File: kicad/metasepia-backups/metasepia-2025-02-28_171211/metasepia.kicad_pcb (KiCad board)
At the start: 2 copper layers, 227.4 x 131.5 mm, 63 parts

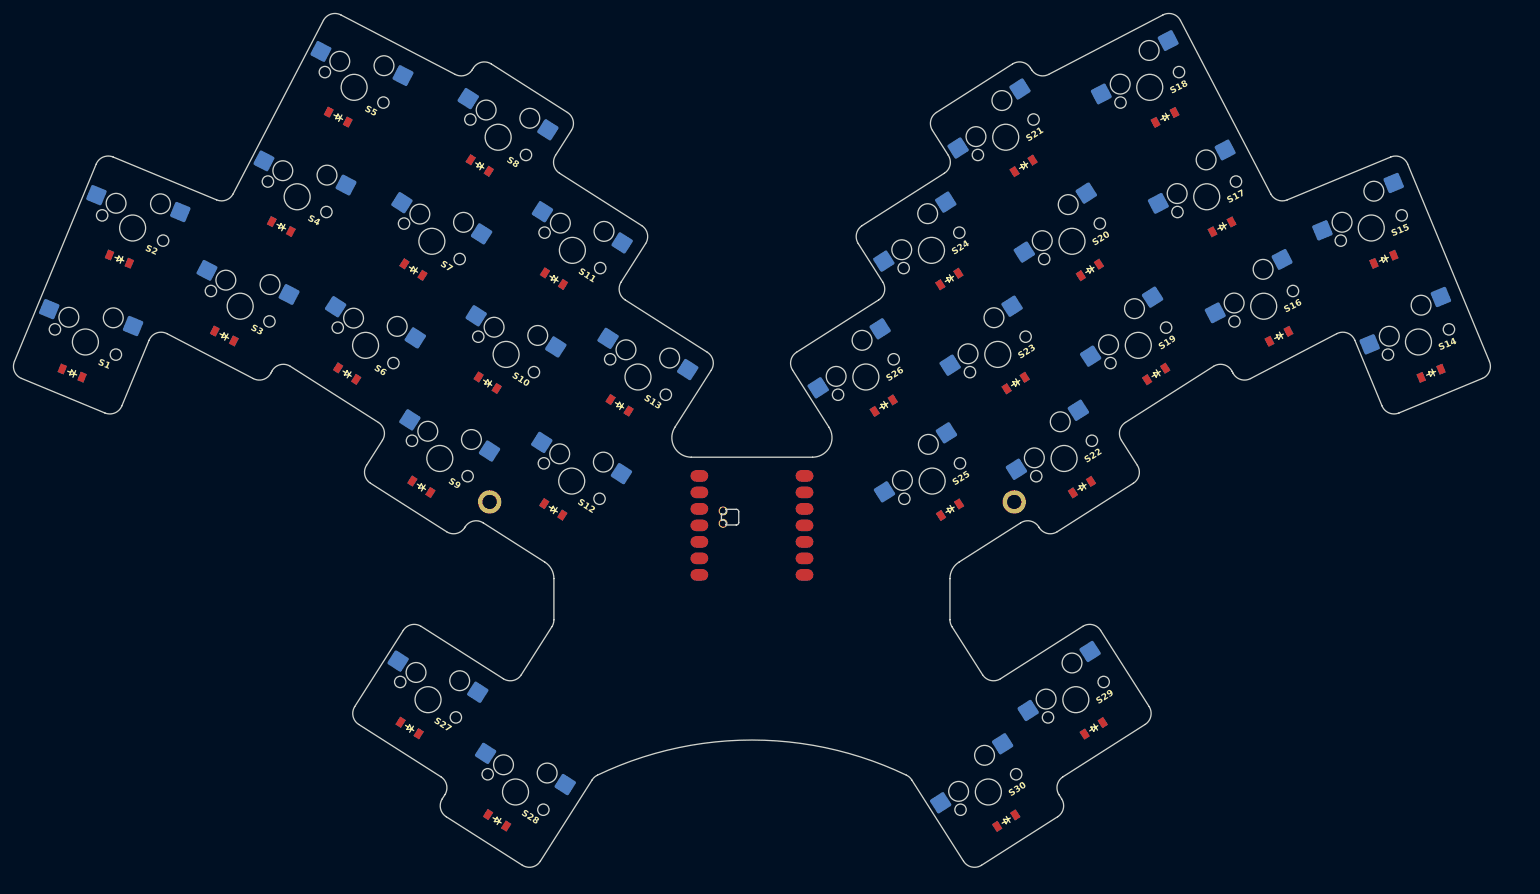
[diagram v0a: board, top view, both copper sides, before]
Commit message: beginning routing in kicad. Minor footprint edits.
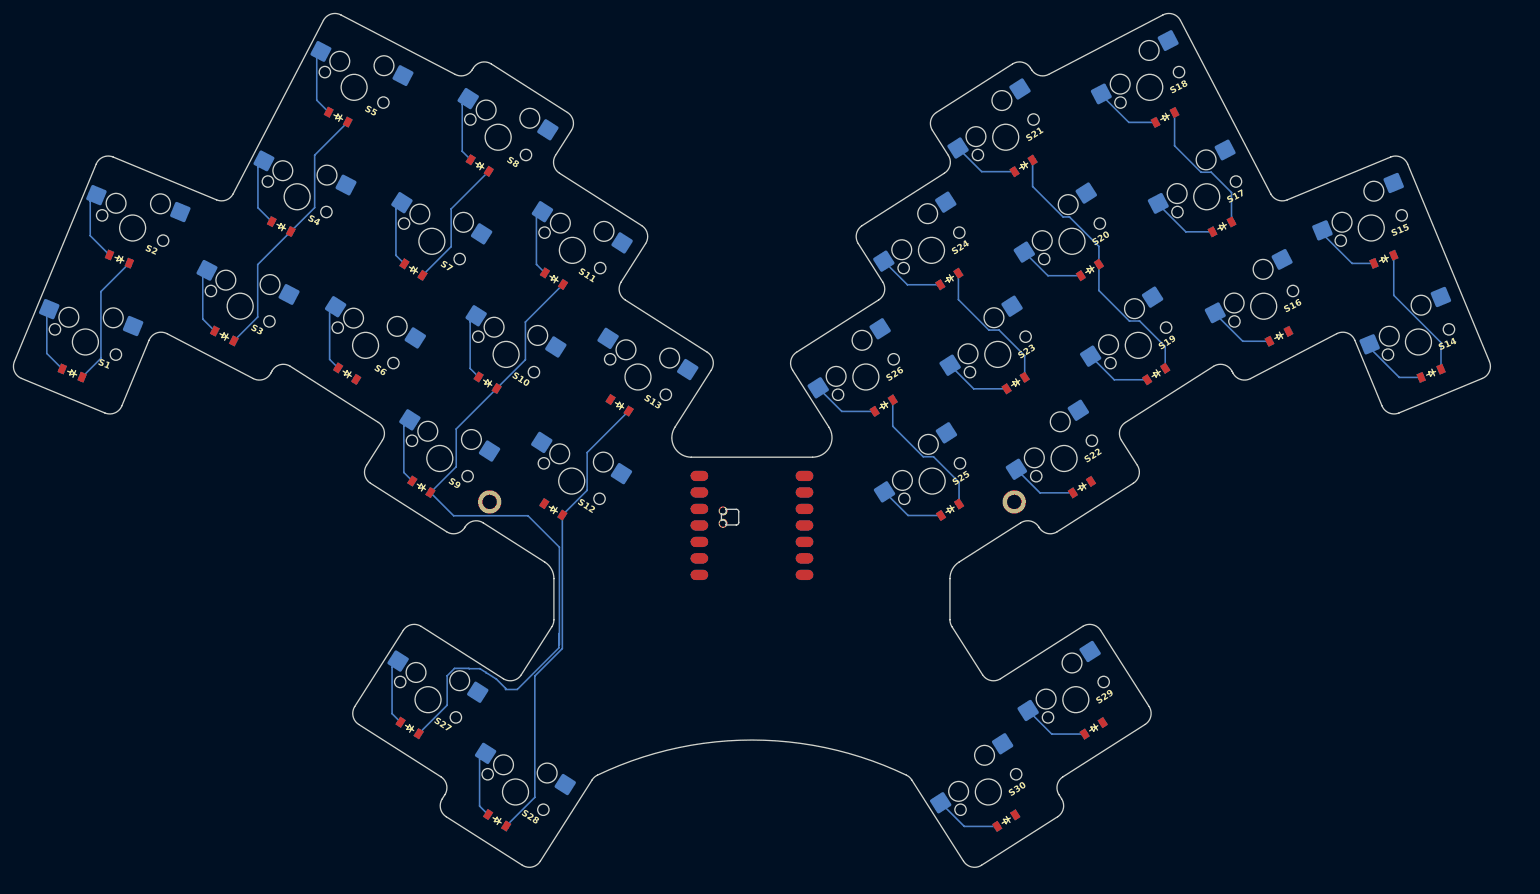
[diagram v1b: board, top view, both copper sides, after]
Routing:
- net P7: track 0.00 -> 133.6 mm
- net P8: track 0.00 -> 92.9 mm
- net P9: track 0.00 -> 63.2 mm
- net P6: track 0.00 -> 61.5 mm
- net P10: track 0.00 -> 42.0 mm
- net pinky_home: track 0.00 -> 10.8 mm
- net ring_home: track 0.00 -> 10.6 mm
- net middle_bottom: track 0.00 -> 10.3 mm
- net middle_top: track 0.00 -> 10.3 mm
- net index_home: track 0.00 -> 10.3 mm
- net index_bottom: track 0.00 -> 10.3 mm
- net middle_home: track 0.00 -> 10.3 mm
- net reachy_default: track 0.00 -> 10.3 mm
- net tucky_default: track 0.00 -> 10.3 mm
- net index_top: track 0.00 -> 10.3 mm
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
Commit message: routed, badly. All diodes are fucked. Need redo.
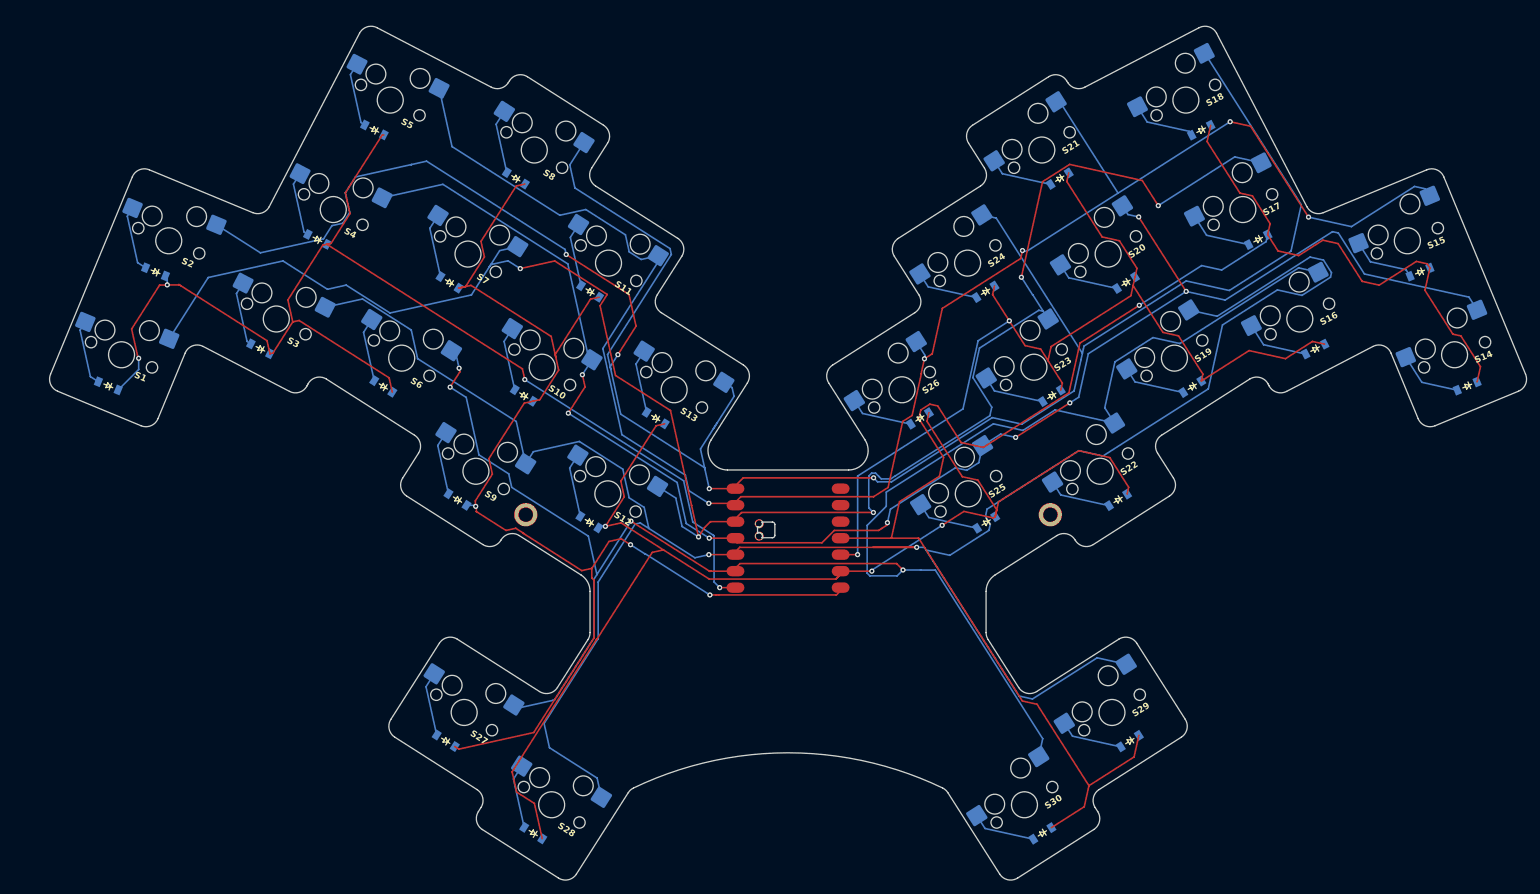
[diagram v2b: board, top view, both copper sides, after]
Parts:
- moved D14 5.90 mm to (253.9, 81.9)
- moved S25 5.90 mm to (177.1, 98.7)
- moved S1 5.90 mm to (46.7, 77.3)
- moved D30 5.90 mm to (188.4, 150.8)
- moved S21 5.90 mm to (188.4, 45.7)
- moved S13 5.90 mm to (131.8, 82.7)
- moved S12 5.90 mm to (121.5, 98.7)
- moved S19 5.90 mm to (208.8, 77.8)
- moved S5 5.90 mm to (88.0, 38.0)
- moved D1 5.90 mm to (44.7, 81.9)
- moved D20 5.90 mm to (201.3, 66.0)
- moved S18 5.90 mm to (210.6, 38.0)
- moved S10 5.90 mm to (111.4, 79.2)
- moved S2 5.90 mm to (53.9, 59.7)
- moved D29 5.90 mm to (201.9, 136.6)
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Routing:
- net P0: track 0.00 -> 348.3 mm, vias 0 -> 4
- net P4: track 0.00 -> 331.4 mm, vias 0 -> 2
- net P2: track 0.00 -> 281.5 mm, vias 0 -> 5
- net P5: track 0.00 -> 272.8 mm, vias 0 -> 4
- net P1: track 0.00 -> 268.9 mm, vias 0 -> 5
- net P3: track 0.00 -> 249.2 mm, vias 0 -> 8
- net P10: track 42.0 -> 248.5 mm, vias 0 -> 1
- net P6: track 61.5 -> 189.0 mm, vias 0 -> 4
- net P8: track 92.9 -> 189.8 mm, vias 0 -> 3
- net P9: track 63.2 -> 151.1 mm, vias 0 -> 2
- net P7: track 133.6 -> 188.5 mm, vias 0 -> 3
- net inner_home: track 0.00 -> 9.97 mm
- net inner_top: track 0.00 -> 9.97 mm
- net ring_bottom: track 9.47 -> 10.2 mm
- net ring_top: track 9.47 -> 10.2 mm
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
